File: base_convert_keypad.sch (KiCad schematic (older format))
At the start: 40 parts

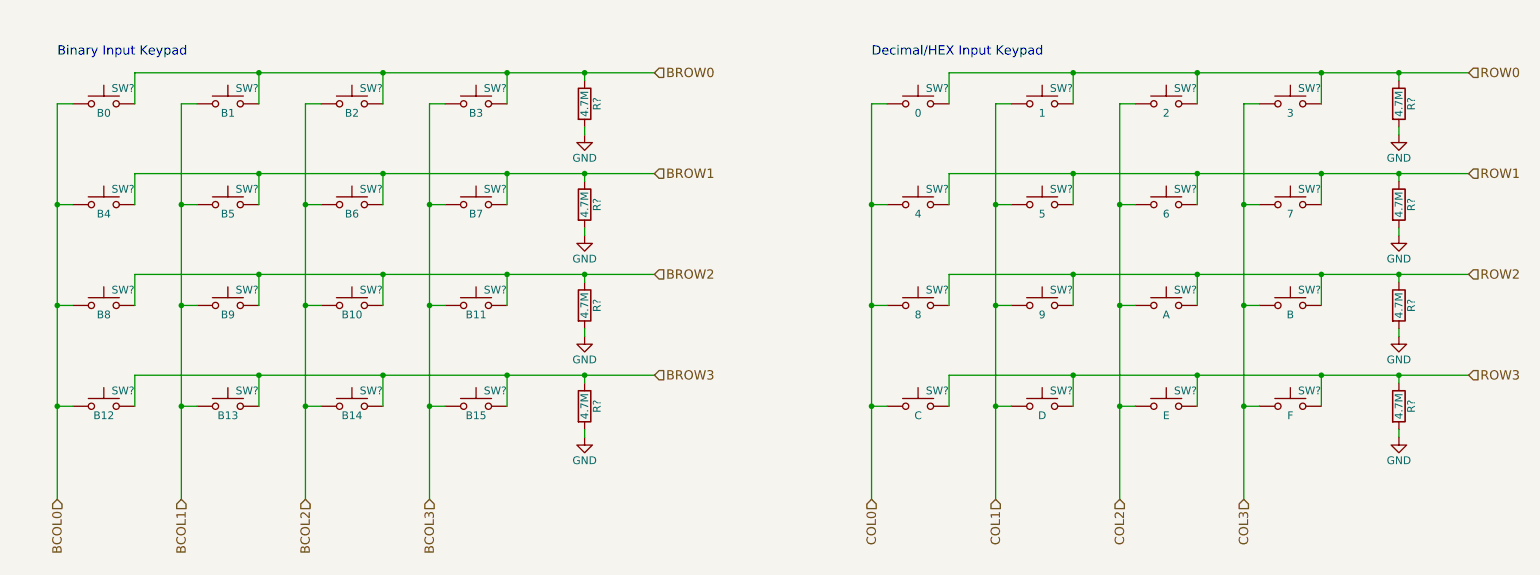
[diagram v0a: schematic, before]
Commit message: schematic captured, footprints complete
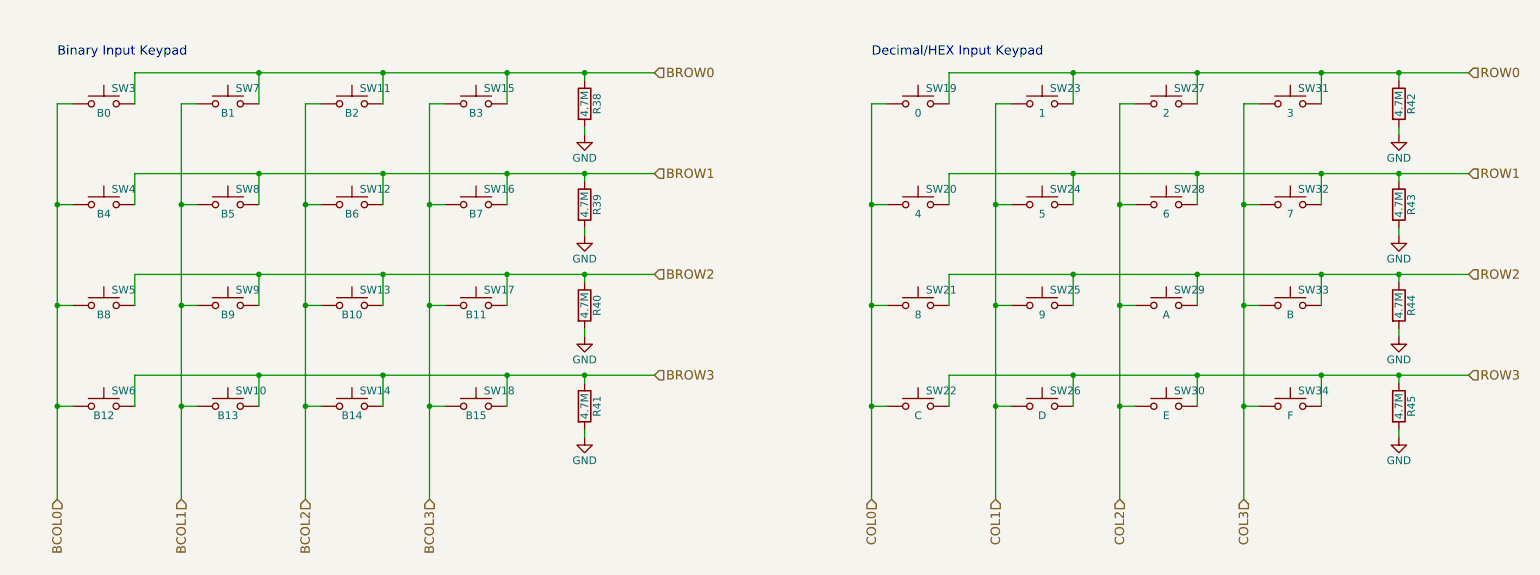
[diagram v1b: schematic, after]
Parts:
- R38, R39, R40, R41, R42, R43, R44, R45: renamed from R?; footprint (none) -> Resistors_SMD:R_0805
- SW10, SW11, SW12, SW13, SW14, SW15, SW16, SW17, SW18, SW19, SW20, SW21, SW22, SW23, SW24, SW25, SW26, SW27, SW28, SW29, SW3, SW30, SW31, SW32, SW33, SW34, SW4, SW5, SW6, SW7, SW8, SW9: renamed from SW?; footprint (none) -> Buttons_Switches_THT:SW_PUSH_6mm

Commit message: remove external pulldown resistors
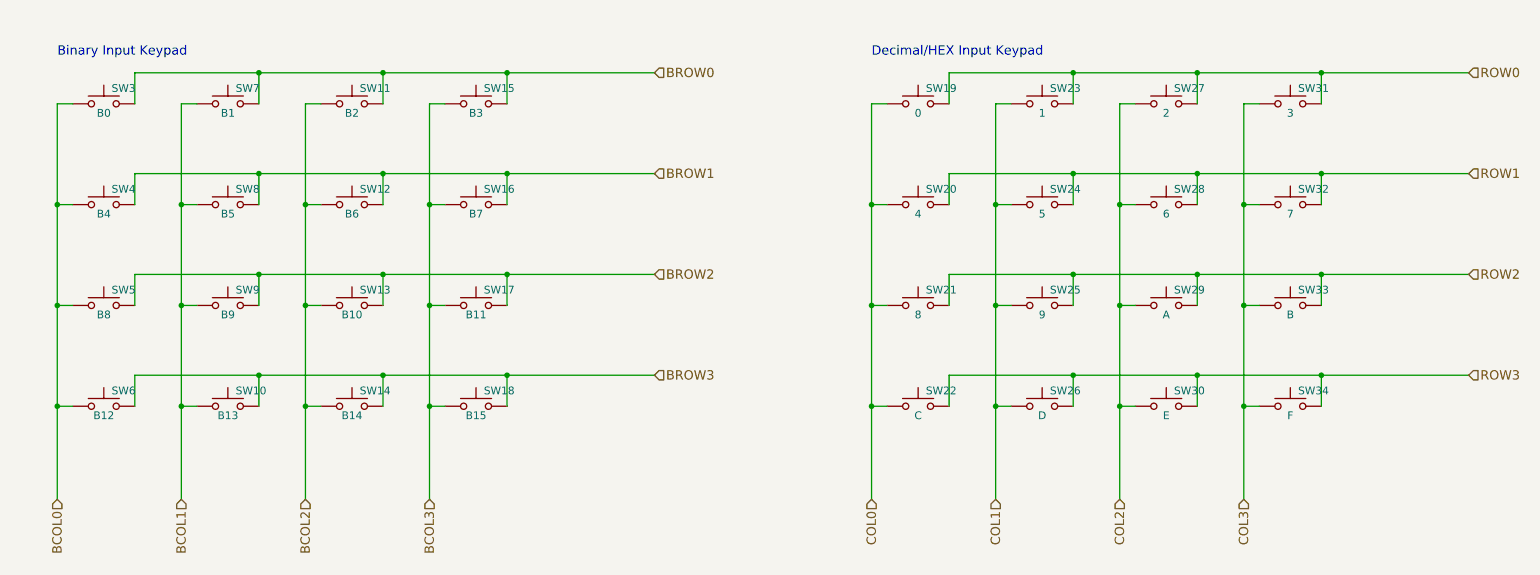
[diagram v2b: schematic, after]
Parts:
- removed R38, R39, R40, R41, R42, R43, R44, R45: 4.7M, Resistors_SMD:R_0805, symbol R

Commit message: updated shema fields. Raplced tack switch with 4 pin footprint
Using 4 pin tack switch to ease pcb layout connecitions. Also updated component fields in schema
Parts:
- SW10, SW11, SW12, SW13, SW14, SW15, SW16, SW17, SW18, SW19, SW20, SW21, SW23, SW24, SW25, SW26, SW27, SW28, SW29, SW3, SW30, SW31, SW32, SW33, SW34, SW4, SW5, SW6, SW7, SW8, SW9: footprint Buttons_Switches_THT:SW_PUSH_6mm -> Buttons_Switches_THT:SW_TH_Tactile_Omron_B3F-10xx; symbol SW_Push -> SW_Push_Dual
- SW22: footprint Buttons_Switches_THT:SW_PUSH_6mm -> Buttons_Switches_THT:SW_TH_Tactile_Omron_B3F-10xx; symbol SW_Push -> SW_Push_Dual; Description (none) -> NONE; Manufacture (none) -> NONE; Mfg Part Number (none) -> NONE; Package (none) -> NONE

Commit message: Push and shove for the win!
To Do: clean up.
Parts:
- SW10, SW11, SW12, SW13, SW14, SW15, SW16, SW17, SW18, SW20, SW21, SW23, SW24, SW25, SW27, SW28, SW3, SW30, SW31, SW34, SW4, SW5, SW6, SW7, SW8, SW9: symbol SW_Push_Dual -> SW_Push_Dual2; Description (none) -> NONE; Manufacture (none) -> NONE; Mfg Part Number (none) -> NONE; Package (none) -> NONE
- SW19: renamed from SW22; value C -> 0; symbol SW_Push_Dual -> SW_Push_Dual2
- SW22: renamed from SW32; value 7 -> C; symbol SW_Push_Dual -> SW_Push_Dual2; Description (none) -> NONE; Manufacture (none) -> NONE; Mfg Part Number (none) -> NONE; Package (none) -> NONE
- SW26: renamed from SW33; value B -> D; symbol SW_Push_Dual -> SW_Push_Dual2; Description (none) -> NONE; Manufacture (none) -> NONE; Mfg Part Number (none) -> NONE; Package (none) -> NONE
- SW29: renamed from SW26; value D -> A; symbol SW_Push_Dual -> SW_Push_Dual2; Description (none) -> NONE; Manufacture (none) -> NONE; Mfg Part Number (none) -> NONE; Package (none) -> NONE
- SW32: renamed from SW29; value A -> 7; symbol SW_Push_Dual -> SW_Push_Dual2; Description (none) -> NONE; Manufacture (none) -> NONE; Mfg Part Number (none) -> NONE; Package (none) -> NONE
- SW33: renamed from SW19; value 0 -> B; symbol SW_Push_Dual -> SW_Push_Dual2; Description (none) -> NONE; Manufacture (none) -> NONE; Mfg Part Number (none) -> NONE; Package (none) -> NONE
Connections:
- wire segments 80 -> 88
